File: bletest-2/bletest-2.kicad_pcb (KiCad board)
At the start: 2 copper layers, 78.5 x 52 mm, 44 parts, among them J1 Conn_01x02, J2 Conn_01x02, J3 Conn_ARM_JTAG_SWD_10, J4 Conn_01x02, J5 Conn_01x02, J6 Conn_01x02, J7 USB_C_Receptacle_USB2.0_16P, SW1 SW_Push, SW2 SW_Push, SW3 SW_Push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

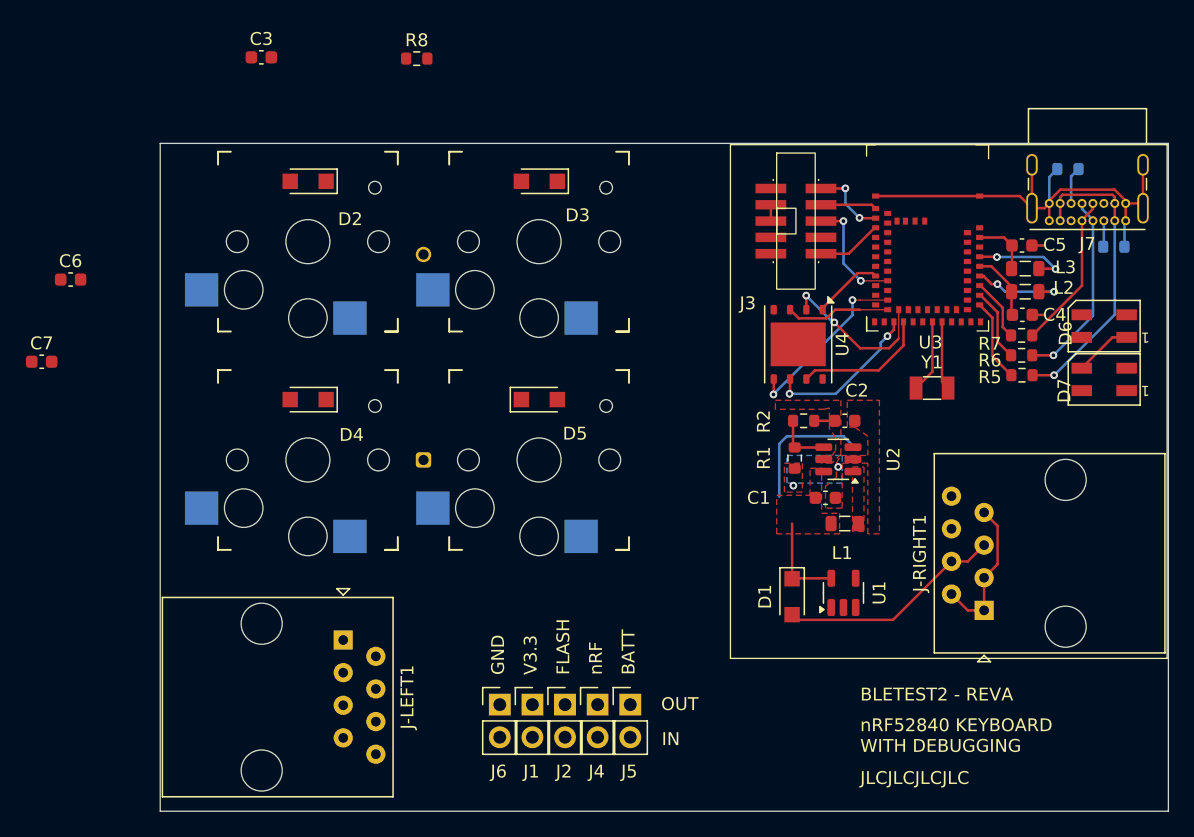
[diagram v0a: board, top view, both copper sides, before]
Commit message: Full routing done
There are still a bunch of ERC violations.
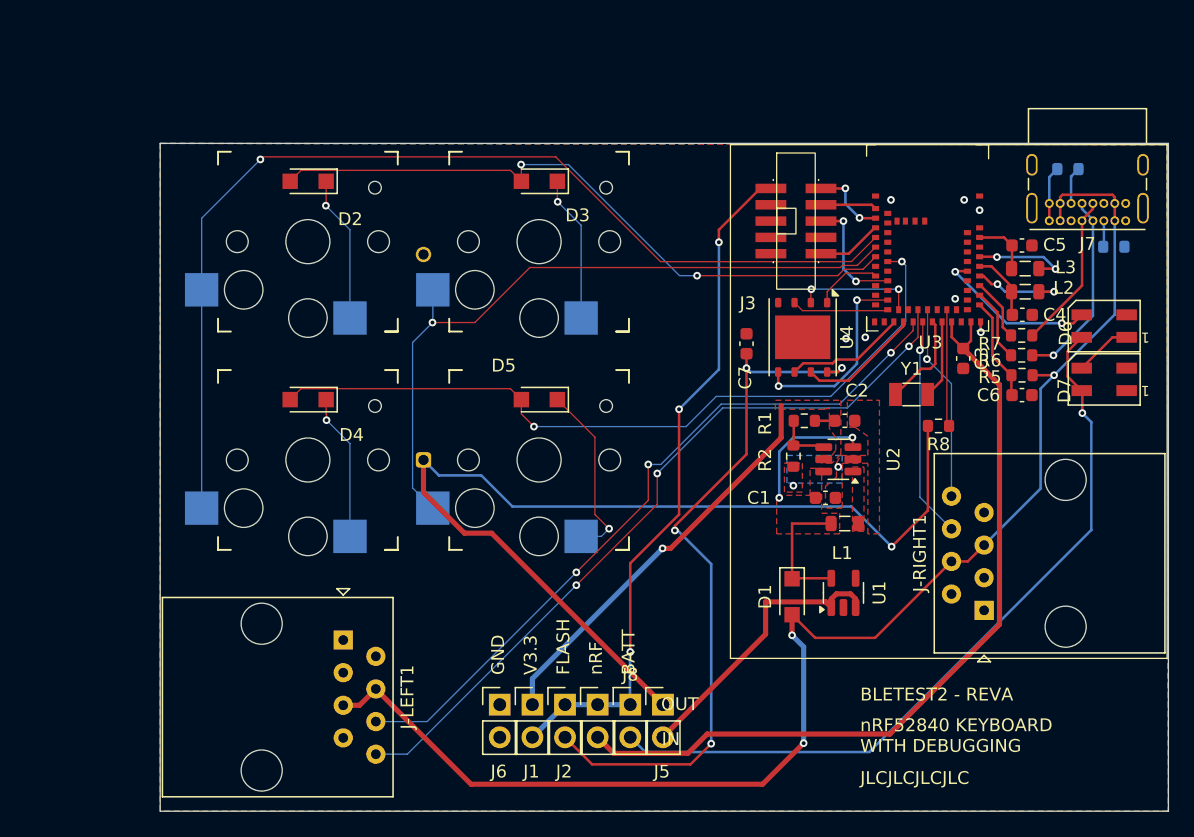
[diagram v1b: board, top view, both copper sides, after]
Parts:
- added J8: Conn_01x02, Connector_PinHeader_2.54mm:PinHeader_1x02_P2.54mm_Vertical, F.Cu at (132.1, 73.7)
- moved C6 74.6 mm to (162.6, 49.6)
- moved C3 59.5 mm to (158.0, 46.8), turned to -90 degrees
- moved C7 54.9 mm to (141.2, 45.6), turned to 90 degrees
- moved R8 49.7 mm to (156.1, 52.0), turned to 180 degrees
- moved R1 3.00 mm to (145.7, 51.6), turned to 180 degrees
- moved R2 2.86 mm to (144.8, 54.4), turned to -90 degrees
- moved J5 2.54 mm to (134.6, 73.7)
- moved Y1 1.68 mm to (154.0, 49.5)
- moved U4 0.65 mm to (145.5, 45.1)
- turned D5 to 180 degrees
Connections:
- D2 pad 2: /Switches/COL-A -> /COL-A
- D3 pad 2: /Switches/COL-A -> /COL-A
- D4 pad 2: /Switches/COL-B -> /COL-B
- D5 pad 2: /Switches/COL-B -> /COL-B
- D6 pad 4: +3.3V -> Net-(D6-VDD)
- D7 pad 4: +3.3V -> Net-(D6-VDD)
- R1 pad 2: Net-(R1-Pad2) -> Net-(U2-FB)
- R2 pad 1: Net-(R1-Pad2) -> Net-(U2-FB)
- SW1 pad 2: /Switches/ROW-A -> /ROW-A
- SW2 pad 2: /Switches/ROW-B -> /ROW-B
- SW3 pad 2: /Switches/ROW-A -> /ROW-A
- SW4 pad 2: /Switches/ROW-B -> /ROW-B
- U2 pad 4: unconnected-(U2-FB-Pad4) -> Net-(U2-FB)
- U2 pad 5: unconnected-(U2-VOUT-Pad5) -> Net-(J1-Pin_1)
- U3 pad 10: unconnected-(U3F-P1.06-Pad10) -> /ROW-B
- U3 pad 12: unconnected-(U3E-P0.21-Pad12) -> /COL-A
- U3 pad 13: unconnected-(U3E-P0.20-Pad13) -> /COL-B
- U3 pad 30: unconnected-(U3E-P0.03-Pad30) -> /LEFT-RX
- U3 pad 31: unconnected-(U3F-P1.03-Pad31) -> /LEFT-TX
- U3 pad 32: unconnected-(U3E-P0.02-Pad32) -> /RIGHT-TX
- U3 pad 33: unconnected-(U3F-P1.02-Pad33) -> /RIGHT-RX
- U3 pad 51: unconnected-(U3F-P1.13-Pad51) -> /RGB
- U3 pad 8: unconnected-(U3E-P0.24-Pad8) -> /ROW-A
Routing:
- net /ROW-A: track 0.00 -> 81.2 mm, vias 0 -> 1
- net +BATT: track 0.00 -> 77.8 mm, vias 0 -> 1
- net VBUS: track 41.3 -> 109.1 mm, vias 1 -> 3
- net Net-(J4-Pin_2): track 0.00 -> 63.4 mm
- net Net-(D6-VDD): track 0.00 -> 59.8 mm, vias 0 -> 1
- net /COL-B: track 0.00 -> 59.4 mm, vias 0 -> 2
- net /LEFT-TX: track 0.00 -> 59.2 mm, vias 0 -> 3
- net /LEFT-RX: track 0.00 -> 56.8 mm, vias 0 -> 3
- net Net-(J2-Pin_2): track 0.00 -> 55.9 mm, vias 0 -> 4
- net /ROW-B: track 0.00 -> 55.2 mm, vias 0 -> 1
- net +3.3V: track 0.00 -> 53.8 mm, vias 0 -> 3
- net /COL-A: track 0.00 -> 51.8 mm, vias 0 -> 2
- net GND: track 52.0 -> 5.09 mm, vias 2 -> 9
- net Net-(J1-Pin_1): track 6.67 -> 33.2 mm, vias 0 -> 1
- net Net-(J5-Pin_2): track 0.00 -> 22.7 mm
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- added copper zone on F.Cu, net Net-(J1-Pin_1)
- removed copper zone on F.Cu, net +3.3V

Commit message: Clean up most ERC violations
The remaining are silkscreen overlaps or clipping issues.
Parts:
- R3, R4: moved to F.Cu
- moved R3 8.42 mm to (169.8, 39.6)
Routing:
- net Net-(J7-CC2): track 2.91 -> 12.4 mm, vias 0 -> 1

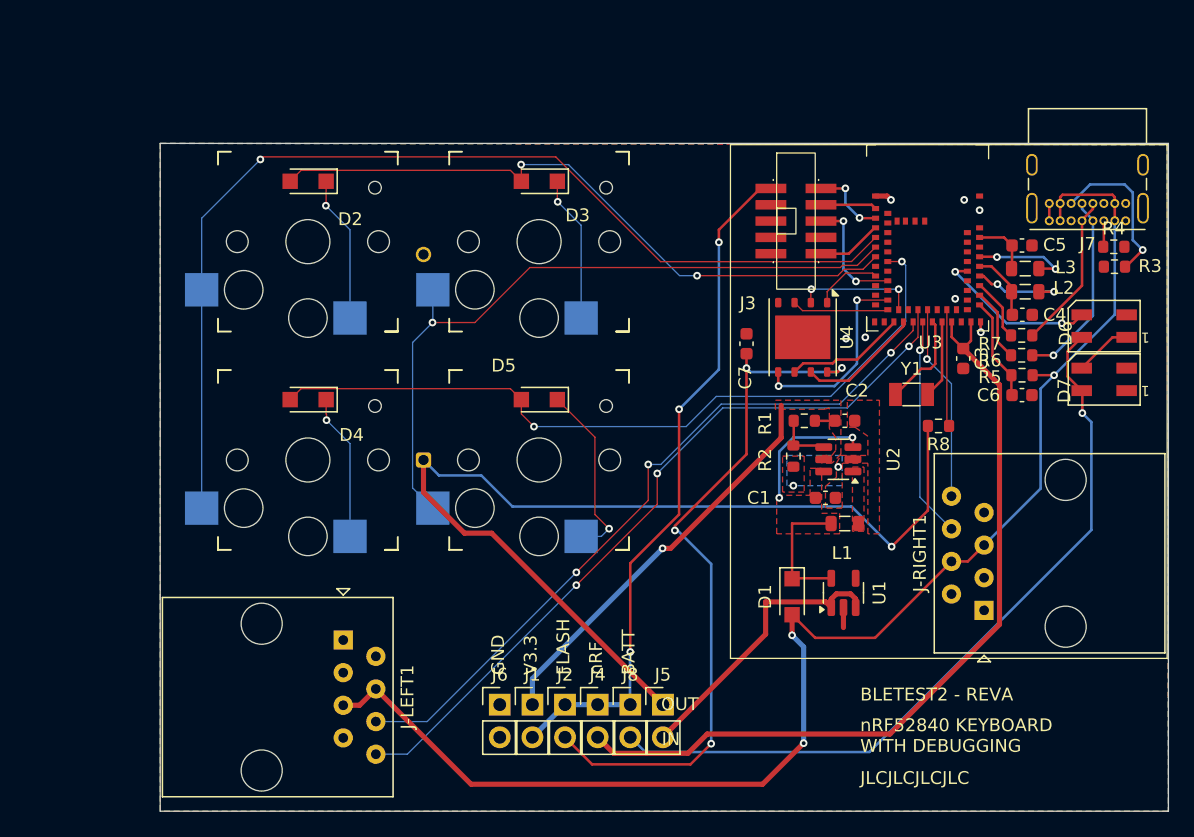
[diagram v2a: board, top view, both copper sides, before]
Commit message: Rev A of bletest
Finish cleanup, and remove last remaining violations.

There are a handful of silkscreen overlaps with explicit exclusions.
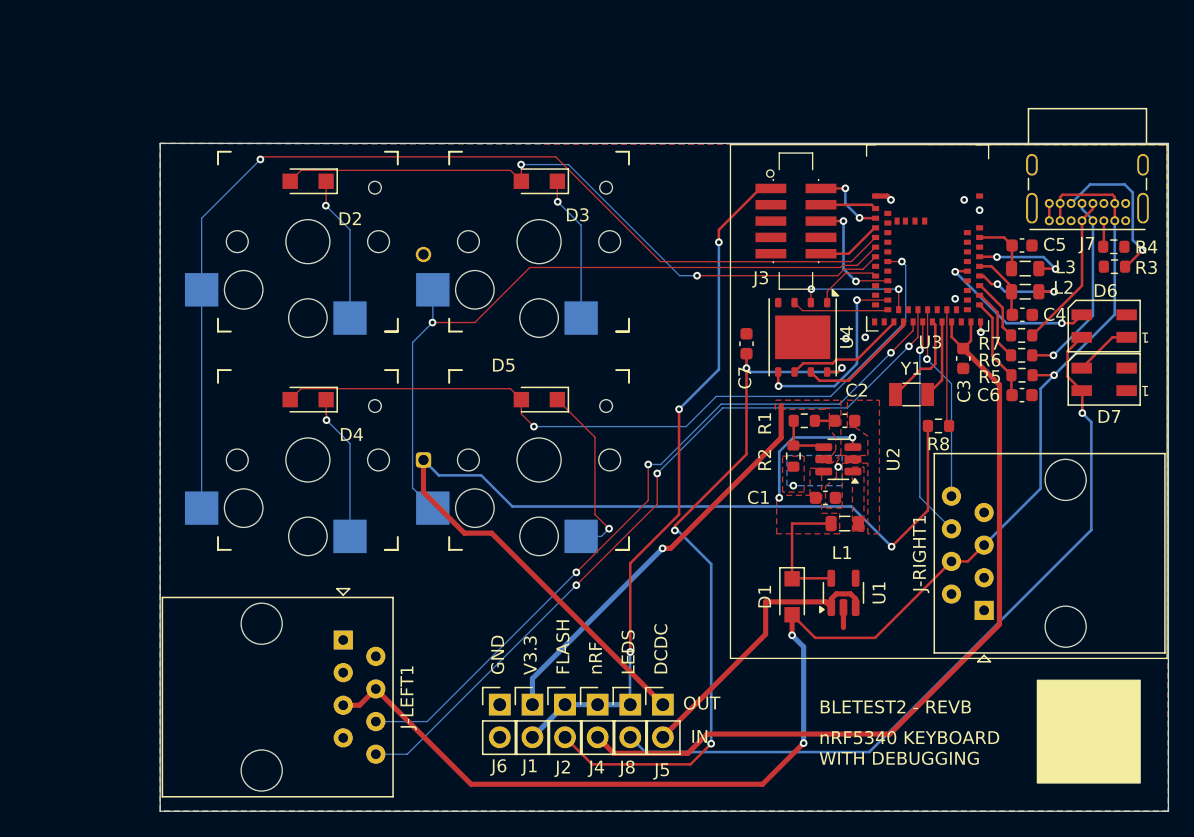
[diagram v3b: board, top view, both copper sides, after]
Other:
- board text added: "BLETEST2 - REVB"
- board text added: "DCDC"
- board text added: "LEDS"
- board text added: "nRF5340 KEYBOARD WITH DEBUGGING"
- board text removed: "BATT"
- board text removed: "BLETEST2 - REVA"
- board text removed: "JLCJLCJLCJLC"
- board text removed: "nRF52840 KEYBOARD WITH DEBUGGING"
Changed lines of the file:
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@@
 		(tags "Through hole pin header THT 1x02 2.54mm single row")
 		(property "Reference" "J2"
-			(at 0 -2.33 0)
+			(at -0.12 4.9 0)
 			(layer "F.SilkS")
 			(effects
@@
 		(tags "capacitor")
 		(property "Reference" "C3"
-			(at 0 -1.43 90)
+			(at 2.55 -0.075 90)
 			(layer "F.SilkS")
 			(effects
@@
 		(tags "Through hole pin header THT 1x02 2.54mm single row")
 		(property "Reference" "J4"
-			(at 0 -2.33 0)
+			(at -0.06 4.9 0)
 			(layer "F.SilkS")
 			(effects
@@
 		(tags "resistor")
 		(property "Reference" "R3"
-			(at -2.775 0.05 360)
+			(at -2.5 -0.1 0)
 			(layer "F.SilkS")
 			(effects
@@
 		)
 		(property "Value" "5.1K"
-			(at 0 1.43 360)
+			(at 0 1.43 0)
 			(layer "F.Fab")
 			(effects
@@
 		)
 		(fp_text user "${REFERENCE}"
-			(at 0 0 360)
+			(at 0 0 0)
 			(layer "F.Fab")
 			(effects
@@
 		(tags "Through hole pin header THT 1x02 2.54mm single row")
 		(property "Reference" "J5"
-			(at 0 -2.33 0)
+			(at -0.04 5.1 0)
 			(layer "F.SilkS")
 			(effects
@@
 		(tags "resistor")
 		(property "Reference" "R4"
-			(at 0 -1.43 360)
+			(at 2.55 0.05 0)
 			(layer "F.SilkS")
 			(effects
@@
 		)
 		(property "Value" "5.1K"
-			(at 0 1.43 360)
+			(at 0 1.43 0)
 			(layer "F.Fab")
 			(effects
@@
 		)
 		(fp_text user "${REFERENCE}"
-			(at 0 0 360)
+			(at 0 0 0)
 			(layer "F.Fab")
 			(effects
@@
 		(tags "Through hole pin header THT 1x02 2.54mm single row")
 		(property "Reference" "J6"
-			(at 0 -2.33 0)
+			(at -0.04 4.8 0)
 			(layer "F.SilkS")
 			(effects
@@
 		(tags "LED RGB NeoPixel Mini PLCC-4 3535")
 		(property "Reference" "D7"
-			(at 3.1 -0.875 90)
+			(at -0.4 -2.925 180)
 			(layer "F.SilkS")
 			(effects
@@
 		(tags "Through hole pin header THT 1x02 2.54mm single row")
 		(property "Reference" "J1"
-			(at 0 -2.33 0)
+			(at -0.18 4.8 0)
 			(layer "F.SilkS")
 			(effects
@@
 		(tags "LED RGB NeoPixel Mini PLCC-4 3535")
 		(property "Reference" "D6"
-			(at 3 -0.575 90)
+			(at -0.1 2.725 180)
 			(layer "F.SilkS")
 			(effects
@@
 		(tags "Through hole pin header THT 1x02 2.54mm single row")
 		(property "Reference" "J8"
-			(at 0 -2.33 0)
+			(at -0.2 4.9 0)
 			(layer "F.SilkS")
 			(effects
@@
 		(tags "Surface mounted pin header SMD 2x05 1.27mm double row")
 		(property "Reference" "J3"
-			(at -3.75 6.4 0)
+			(at -2.7 4.45 0)
 			(layer "F.SilkS")
 			(effects
@@
 		)
 		(fp_line
+			(start -1.3 -5.3)
+			(end 1.3 -5.3)
+			(stroke
+				(width 0.1)
+				(type default)
+			)
+			(layer "F.SilkS")
+		)
+		(fp_line
+			(start -1.3 -4)
+			(end -1.3 -5.3)
+			(stroke
+				(width 0.1)
+				(type default)
+			)
+			(layer "F.SilkS")
+		)
+		(fp_line
+			(start -1.3 4)
+			(end -1.3 5.3)
+			(stroke
+				(width 0.1)
+				(type default)
+			)
+			(layer "F.SilkS")
+		)
+		(fp_line
+			(start -1.3 5.3)
+			(end 1.3 5.3)
+			(stroke
+				(width 0.1)
+				(type default)
+			)
+			(layer "F.SilkS")
+		)
+		(fp_line
+			(start 1.3 -5.3)
+			(end 1.3 -4)
+			(stroke
+				(width 0.1)
+				(type default)
+			)
+			(layer "F.SilkS")
+		)
+		(fp_line
+			(start 1.3 5.3)
+			(end 1.3 4)
+			(stroke
+				(width 0.1)
+				(type default)
+			)
+			(layer "F.SilkS")
+		)
+		(fp_line
 			(start 1.765 -3.235)
 			(end 1.765 -3.17)
@@
 			(layer "F.SilkS")
 		)
-		(fp_rect
-			(start -1.5 -5.3)
-			(end 1.5 5.3)
-			(stroke
-				(width 0.1)
-				(type default)
-			)
-			(fill none)
-			(layer "F.SilkS")
-		)
-		(fp_rect
-			(start -1.5 -1)
-			(end 0 1)
+		(fp_circle
+			(center -2 -3.7)
+			(end -1.8 -3.9)
 			(stroke
 				(width 0.1)
@@
 	)
 	(gr_rect
+		(start 163.8 71.8)
+		(end 171.8 79.8)
+		(stroke
+			(width 0.1)
+			(type solid)
+		)
+		(fill solid)
+		(layer "F.SilkS")
+	)
+	(gr_rect
 		(start 139.9 30.1)
 		(end 173.9 70.1)
@@
 		)
 	)
-	(gr_text "nRF52840 KEYBOARD\nWITH DEBUGGING"
-		(at 150 77.5 0)
+	(gr_text "nRF5340 KEYBOARD\nWITH DEBUGGING"
+		(at 146.8 78.5 0)
 		(layer "F.SilkS")
 		(effects
@@
 		)
 	)
-	(gr_text "JLCJLCJLCJLC"
-		(at 150 80 0)
+	(gr_text "GND"
+		(at 122.391204 71.392832 90)
 		(layer "F.SilkS")
 		(effects
@@
 		)
 	)
-	(gr_text "GND"
-		(at 122.391204 71.392832 90)
+	(gr_text "OUT"
+		(at 136.2 74.2 0)
 		(layer "F.SilkS")
 		(effects
@@
 		)
 	)
-	(gr_text "OUT"
-		(at 134.494294 74.244379 0)
+	(gr_text "BLETEST2 - REVB"
+		(at 146.8 74.5 0)
 		(layer "F.SilkS")
 		(effects
 			(font
 				(size 1 1)
-				(thickness 0.1)
+				(thickness 0.15)
 			)
 			(justify left bottom)
 		)
 	)
-	(gr_text "BLETEST2 - REVA"
-		(at 150 73.5 0)
+	(gr_text "LEDS"
+		(at 132.551204 71.392832 90)
 		(layer "F.SilkS")
 		(effects
 			(font
 				(size 1 1)
-				(thickness 0.15)
+				(thickness 0.1)
 			)
 			(justify left bottom)
 		)
 	)
-	(gr_text "BATT"
-		(at 132.551204 71.392832 90)
+	(gr_text "IN"
+		(at 136.8 76.8 0)
 		(layer "F.SilkS")
 		(effects
@@
 		)
 	)
-	(gr_text "IN"
-		(at 134.544764 76.969752 0)
+	(gr_text "DCDC"
+		(at 135.1 71.4 90)
 		(layer "F.SilkS")
 		(effects
@@
 			(thermal_gap 0.5)
 			(thermal_bridge_width 0.5)
-			(smoothing fillet)
-			(radius 0.1)
 			(island_removal_mode 1)
 			(island_area_min 10)
